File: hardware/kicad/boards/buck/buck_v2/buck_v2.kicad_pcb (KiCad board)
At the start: 2 copper layers, 104 x 104 mm, 31 parts, among them J2 MCP PWM, J3 Conn_01x02_Socket, J5 drive +15V, Q1 IRF530, SW1 Switch, U1 LM7805, U2 NE555, U3 4N25, U4 IR2110

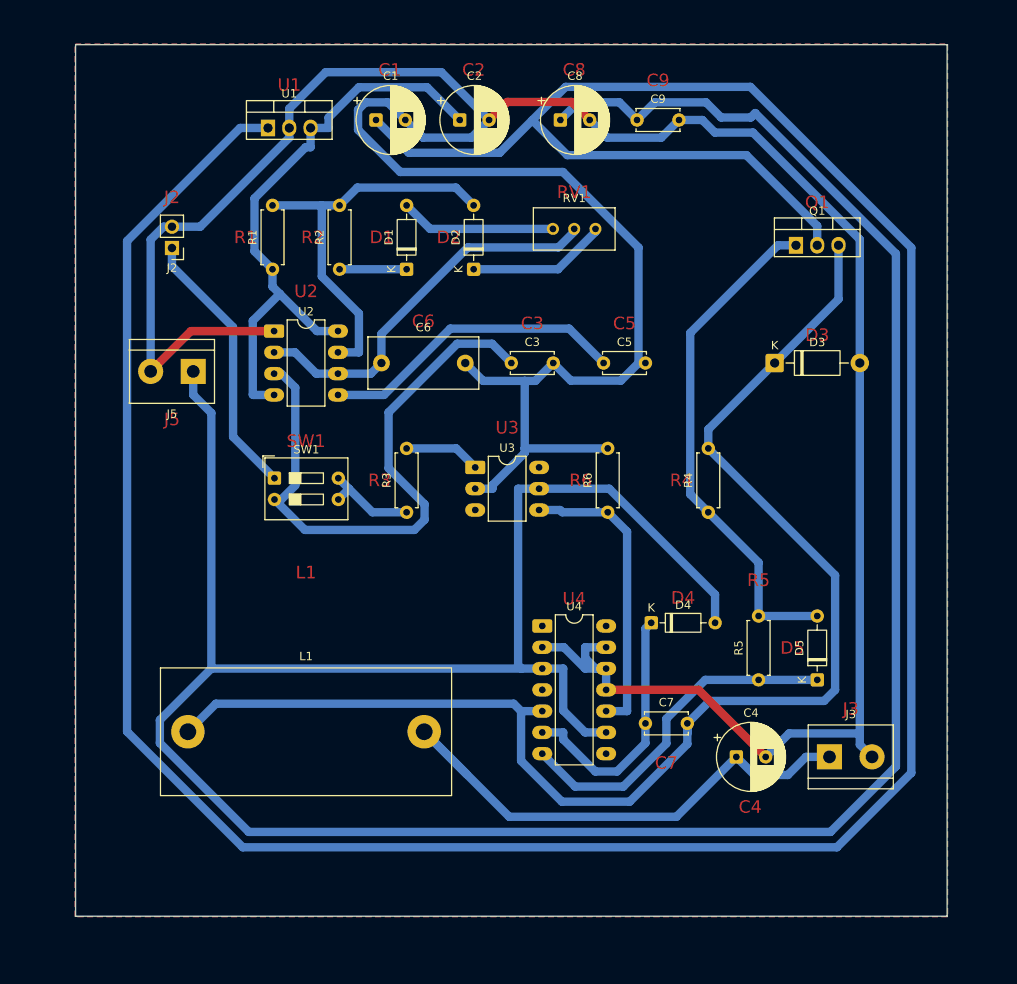
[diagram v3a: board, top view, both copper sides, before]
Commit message: system PCB: routing prep (track 1.0, GND pour both layers) + board/CAM updates
system board:
- fix Default netclass track 0.9 -> 1.0 mm (was below min_track_width, every
  trace would have failed DRC); clearance 1.0, via 2.4/1.0 in .kicad_pro + board
- pour GND on F.Cu and B.Cu (edge inset 0.5 mm, solid pad tie)
- routing tooling: route_prep (netclass+pour), export_dsn_noplane (route GND as
  tracks; Freerouting 1.9.0 chokes on full-board planes), route_finish (SES
  import + refill + sparse GND stitching), inspect_system

srm-cam: bump submodule to double-sided support (90 rotation, bottom-side bed
leveling, GUI ruler/STOP/probe-grid, run-time estimator)

production: rename boost_v2_mill nc -> board_*, add drive_circuit trace rework
boards: buck_v2, current_sense, c2000_feedback edits; BOM + AD3 lab-guide
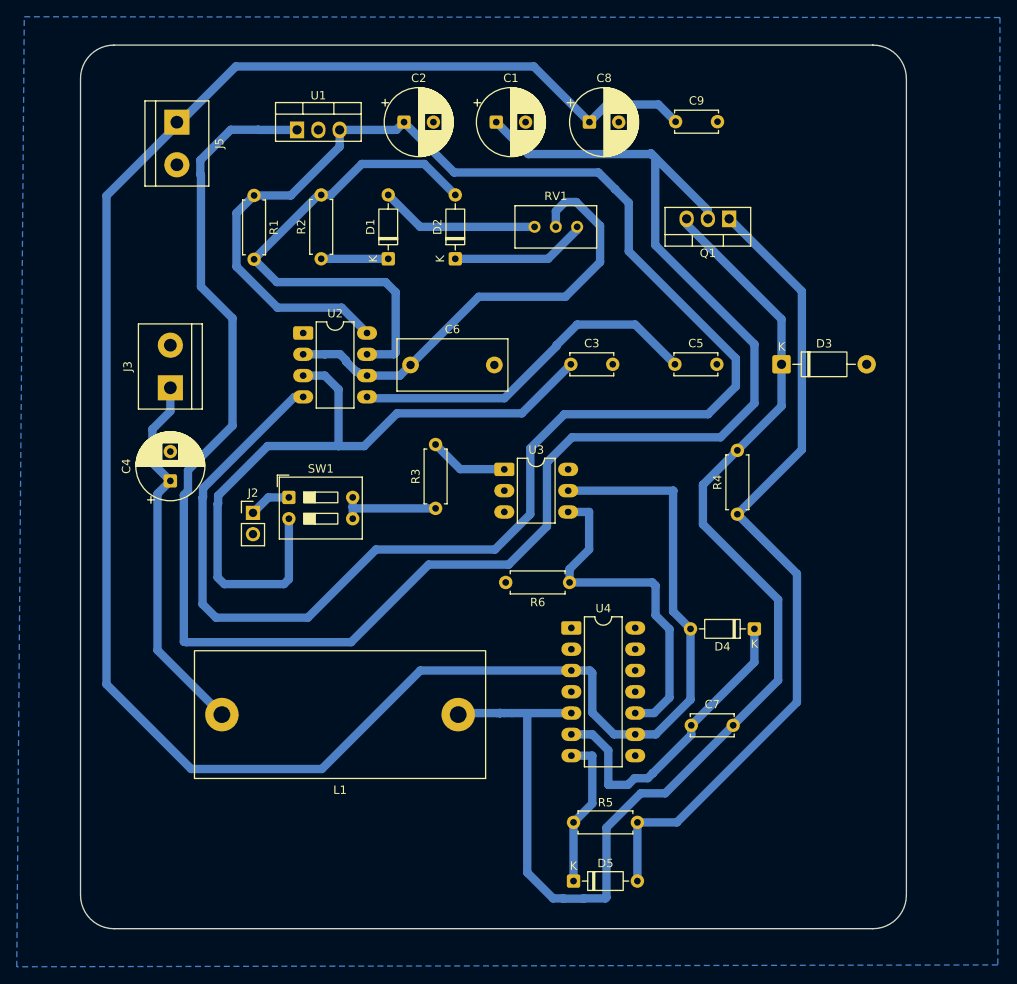
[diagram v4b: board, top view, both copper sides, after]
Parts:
- moved J3 90.1 mm to (31.3, 60.9), turned to 90 degrees
- moved C4 75.1 mm to (31.3, 72.1), turned to 90 degrees
- moved D5 37.7 mm to (79.4, 119.8), turned to 0 degrees
- moved J2 33.1 mm to (41.2, 75.9), turned to 0 degrees
- moved L1 32.3 mm to (65.7, 99.9), turned to 180 degrees
- moved J5 29.8 mm to (32.1, 29.3), turned to -90 degrees
- moved R5 27.9 mm to (79.4, 112.8), turned to 0 degrees
- moved C1 14.4 mm to (70.2, 29.2)
- moved D4 12.3 mm to (101.0, 89.7), turned to 180 degrees
- moved R6 9.53 mm to (79.0, 84.2), turned to 180 degrees
- moved R1 9.08 mm to (41.3, 38.0), turned to -90 degrees
- moved Q1 8.57 mm to (98.0, 40.8), turned to 180 degrees
- moved C5 8.52 mm to (91.5, 58.1)
- moved C3 7.10 mm to (79.1, 58.1)
- moved C2 6.65 mm to (59.2, 29.2)
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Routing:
- net /GND: track 378.5 -> 0.00 mm
- net Net-(U1-VO): track 71.0 -> 219.6 mm
- net Rectifier: track 364.8 -> 224.6 mm
- net /+15V: track 361.9 -> 262.2 mm
- net /GATE: track 61.1 -> 99.4 mm
- net Net-(J2-Pin_1): track 32.5 -> 5.05 mm
- net /HO: track 41.4 -> 18.4 mm
- net Net-(J3-Pin_1): track 64.5 -> 44.6 mm
- net /SW: track 163.4 -> 146.9 mm
- net Net-(U2-OUT): track 71.6 -> 86.3 mm
- net Net-(D2-A): track 47.6 -> 59.5 mm
- net Net-(U2-THRES): track 46.3 -> 55.3 mm
- net /VB: track 30.8 -> 37.8 mm
- net Net-(U2-CONT): track 36.7 -> 42.5 mm
- net /HIN: track 35.5 -> 41.2 mm
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- added copper zone on B.Cu, net /GND
- removed copper zone on B.Cu, net (none)
- removed copper zone on F.Cu, net (none)
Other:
- board size 104 x 104 mm -> 98.5 x 105.4 mm
- board text removed: "C1"
- board text removed: "C2"
- board text removed: "C3"
- board text removed: "C4"
- board text removed: "C5"
- board text removed: "C6"
- board text removed: "C7"
- board text removed: "C8"
- board text removed: "C9"
- board text removed: "D1"
- board text removed: "D2"
- board text removed: "D3"
- board text removed: "D4"
- board text removed: "D5"
- board text removed: "J2"
- board text removed: "J3"
- board text removed: "J5"
- board text removed: "L1"
- board text removed: "Q1"
- board text removed: "R1"
- board text removed: "R2"
- board text removed: "R3"
- board text removed: "R4"
- board text removed: "R5"
- board text removed: "R6"
- board text removed: "RV1"
- board text removed: "SW1"
- board text removed: "U1"
- board text removed: "U2"
- board text removed: "U3"
- board text removed: "U4"
